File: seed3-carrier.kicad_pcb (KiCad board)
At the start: 2 copper layers, 49 parts, among them J1 AudioJack2, J2 AudioJack2, J3 5V_IN, J4 DISPLAY_UART, J5 SJ1-3535NG, U1 TLV9062IDR, U2 TPA6111A2DR

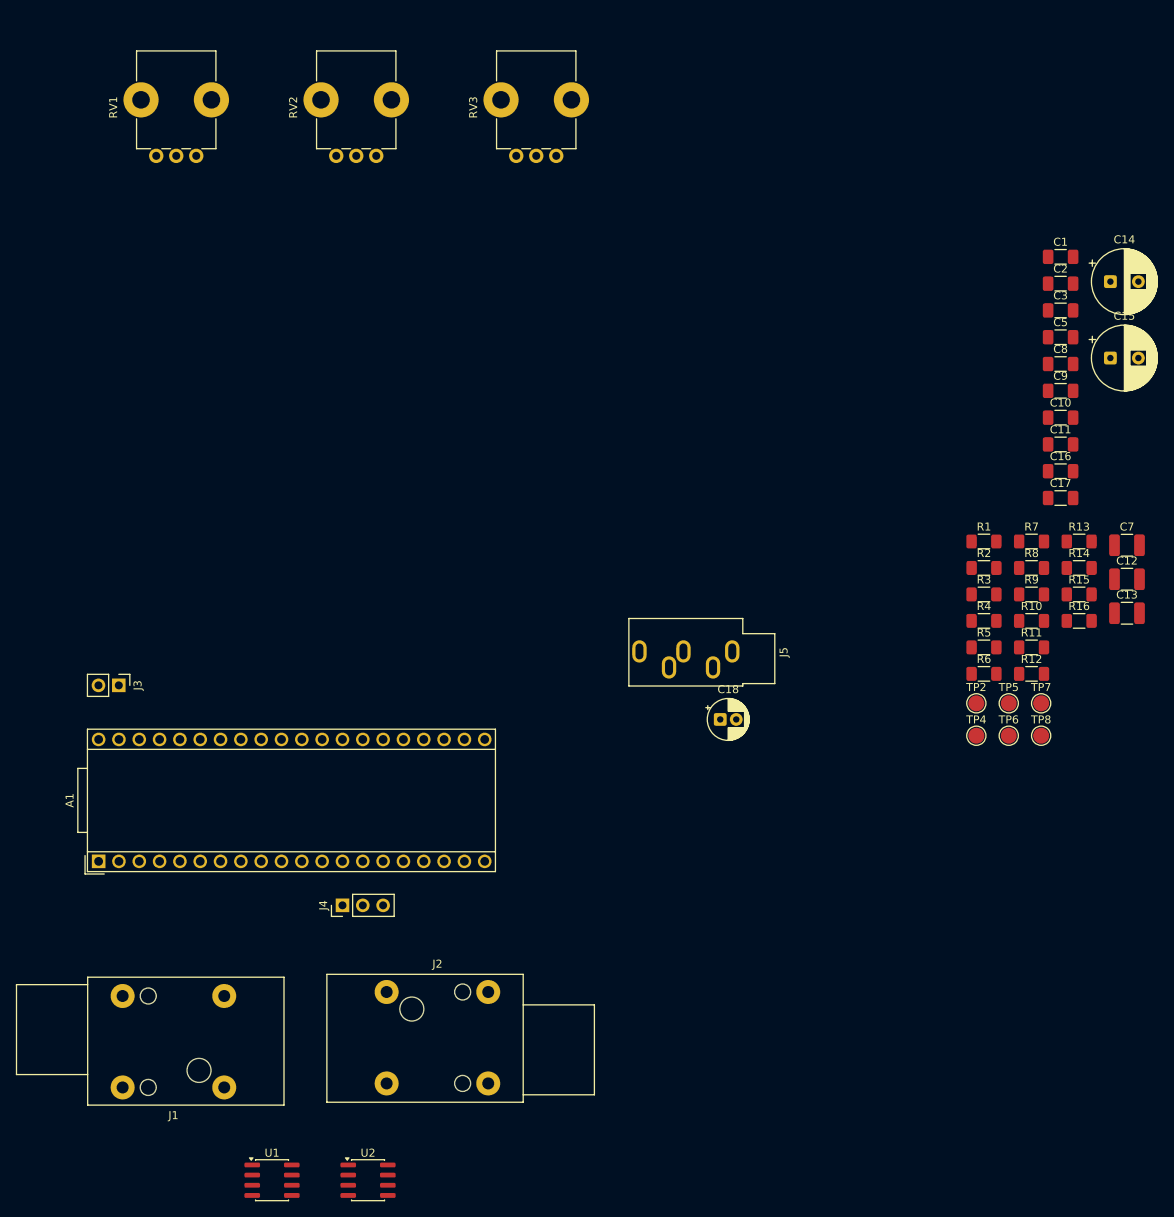
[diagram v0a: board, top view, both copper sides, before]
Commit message: Save initial PCB placement checkpoint
Capture preliminary component placement and schematic testpoint updates. Placement remains in progress; no copper traces or vias have been routed.
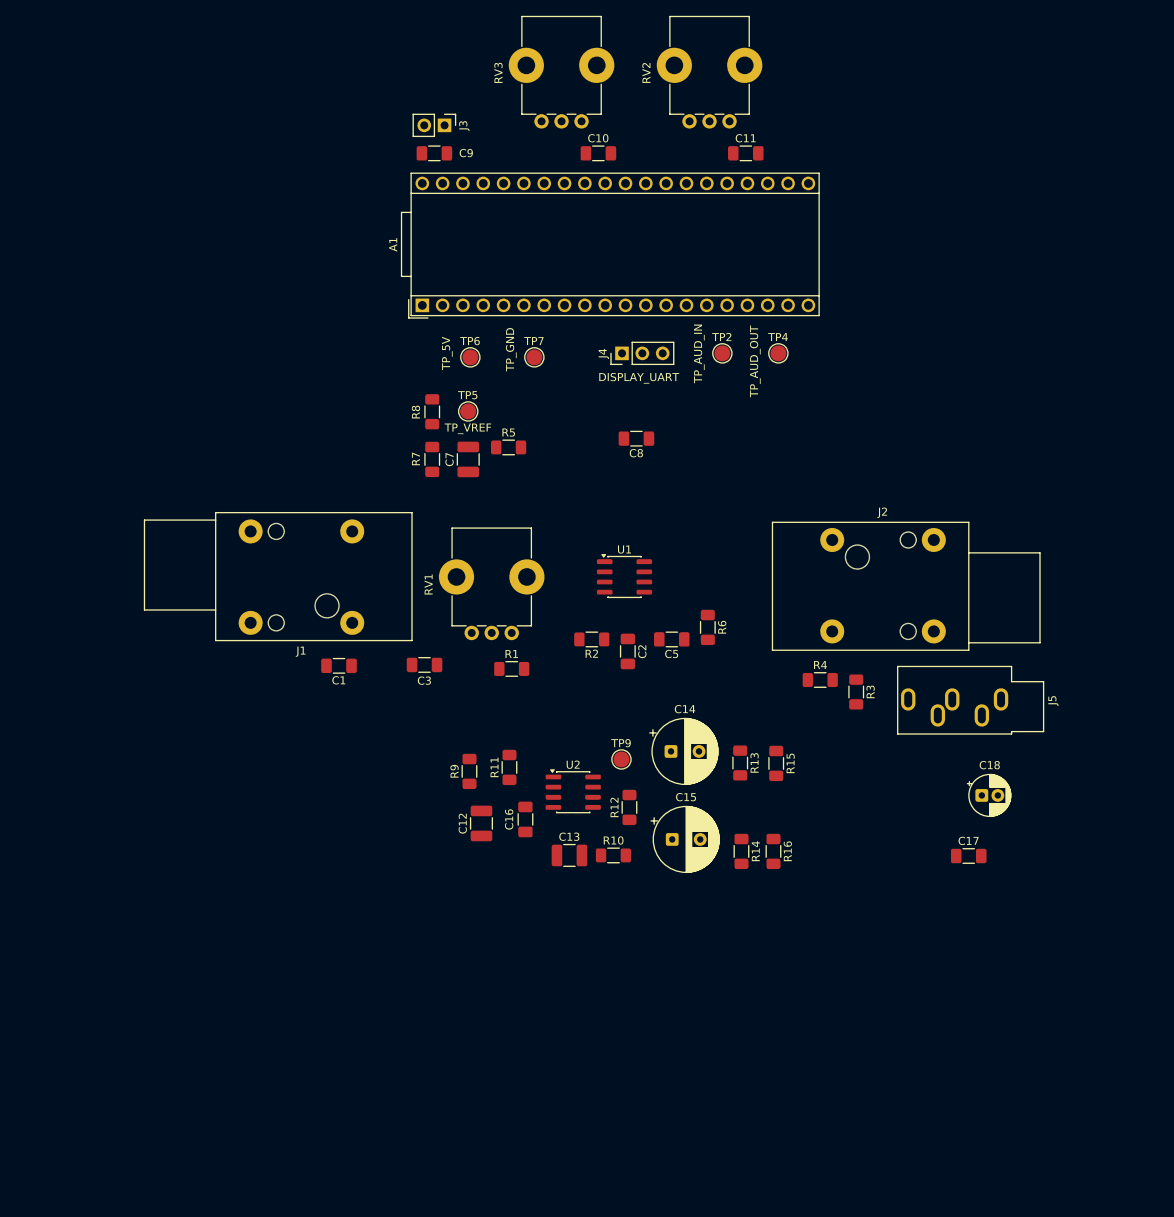
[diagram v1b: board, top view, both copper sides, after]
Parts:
- removed TP8: TestPoint, TestPoint:TestPoint_Pad_D2.0mm
- added TP9: TP_AMP_5V, TestPoint:TestPoint_Pad_D2.0mm, F.Cu at (114.7, 123.0)
- TP2: value TestPoint -> TP_AUD_IN
- TP4: value TestPoint -> TP_AUD_OUT
- TP5: value TestPoint -> TP_VREF
- TP6: value TestPoint -> TP_5V
- TP7: value TestPoint -> TP_GND
- moved C1 103.7 mm to (79.3, 111.3), turned to 180 degrees
- moved C3 91.0 mm to (90.0, 111.2)
- moved U1 87.3 mm to (115.0, 100.2)
- moved C12 86.3 mm to (97.2, 131.0), turned to 90 degrees
- moved C9 83.7 mm to (91.3, 47.2)
- moved C7 83.0 mm to (95.5, 85.5), turned to 90 degrees
- moved TP6 82.3 mm to (95.8, 72.7)
- moved C15 81.4 mm to (121.0, 133.0)
- moved J3 81.0 mm to (92.5, 43.7)
- moved A1 80.4 mm to (89.8, 66.2)
- moved C14 80.4 mm to (120.8, 122.0)
- moved C16 79.8 mm to (102.7, 130.5), turned to -90 degrees
- moved J2 79.3 mm to (141.0, 95.6)
- moved R8 77.4 mm to (91.0, 79.5), turned to -90 degrees
- moved J4 77.3 mm to (114.7, 72.2)
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
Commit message: Save PCB routing progress and Seed3 breakout headers
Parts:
- removed TP2: TP_AUD_IN, TestPoint:TestPoint_Pad_D2.0mm
- removed TP4: TP_AUD_OUT, TestPoint:TestPoint_Pad_D2.0mm
- removed TP6: TP_5V, TestPoint:TestPoint_Pad_D2.0mm
- removed TP7: TP_GND, TestPoint:TestPoint_Pad_D2.0mm
- added J6: Seed3_PINS_RIGHT, Connector_PinSocket_2.54mm:PinSocket_1x20_P2.54mm_Vertical, F.Cu at (101.0, 71.8)
- added J7: Seed3_PINS_LEFT, Connector_PinSocket_2.54mm:PinSocket_1x20_P2.54mm_Vertical, F.Cu at (101.0, 48.3)
- moved C17 62.2 mm to (119.4, 86.4), turned to 180 degrees
- moved C18 60.2 mm to (120.3, 81.9), turned to 180 degrees
- moved RV3 50.8 mm to (158.6, 56.9)
- moved C15 48.6 mm to (132.3, 85.7)
- moved C10 47.6 mm to (157.7, 59.7)
- moved R14 46.4 mm to (141.0, 89.5)
- moved R16 46.0 mm to (146.1, 90.2)
- moved C12 39.1 mm to (108.9, 93.7)
- moved C13 39.0 mm to (118.9, 97.5)
- moved R10 39.0 mm to (124.4, 97.5)
- moved R9 38.4 mm to (108.2, 88.2)
- moved R12 38.3 mm to (124.7, 91.8)
- moved R11 38.2 mm to (112.7, 87.7)
- moved C16 38.0 mm to (113.9, 94.2)
- moved TP9 37.8 mm to (125.4, 86.7)
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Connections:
- net /AUDIO_IN renamed /AUDIO_IN_1
- net /AUDIO_OUT renamed /AUDIO_OUT_1
- A1 pad 1: unconnected-(A1-USB_ID-Pad1) -> /D0
- A1 pad 10: unconnected-(A1-SPI1_POCI-Pad10) -> /D9
- A1 pad 11: unconnected-(A1-SPI1_PICO-Pad11) -> /D10
- A1 pad 12: unconnected-(A1-I2C1_SCL-Pad12) -> /D11
- A1 pad 13: unconnected-(A1-I2C1_SDA-Pad13) -> /D12
- A1 pad 17: unconnected-(A1-AUDIO_IN_2-Pad17) -> /AUDIO_IN_2
- A1 pad 19: unconnected-(A1-AUDIO_OUT_2-Pad19) -> /AUDIO_OUT_2
- A1 pad 2: unconnected-(A1-SD_DATA_3-Pad2) -> /D1
- A1 pad 24: unconnected-(A1-ADC_2-Pad24) -> /A2
- A1 pad 25: unconnected-(A1-ADC_3-Pad25) -> /A3
- A1 pad 26: unconnected-(A1-ADC_4-Pad26) -> /A4
- A1 pad 27: unconnected-(A1-ADC_5-Pad27) -> /A5
- A1 pad 28: unconnected-(A1-ADC_6-Pad28) -> /A6
- A1 pad 29: unconnected-(A1-DAC_OUT2-Pad29) -> /A7
- A1 pad 3: unconnected-(A1-SD_DATA_2-Pad3) -> /D2
- A1 pad 30: unconnected-(A1-DAC_OUT1-Pad30) -> /A8
- A1 pad 31: unconnected-(A1-SAI2_MCLK-Pad31) -> /A9
- A1 pad 32: unconnected-(A1-SAI2_SD_B-Pad32) -> /A10
- A1 pad 33: unconnected-(A1-SAI2_SD_A-Pad33) -> /D26
- A1 pad 34: unconnected-(A1-SAI2_FS-Pad34) -> /D27
- A1 pad 35: unconnected-(A1-SAI2_SCK-Pad35) -> /A11
- A1 pad 36: unconnected-(A1-USB_D_--Pad36) -> /USB_D-
- A1 pad 37: unconnected-(A1-USB_D_+-Pad37) -> /USB_D+
- A1 pad 38: unconnected-(A1-3V3_D-Pad38) -> /3V3_D
- A1 pad 4: unconnected-(A1-SD_DATA_1-Pad4) -> /D3
- A1 pad 5: unconnected-(A1-SD_DATA_0-Pad5) -> /D4
- A1 pad 6: unconnected-(A1-SD_CMD-Pad6) -> /D5
- A1 pad 7: unconnected-(A1-SD_CLK-Pad7) -> /D6
- A1 pad 8: unconnected-(A1-SPI1_CS-Pad8) -> /D7
- A1 pad 9: unconnected-(A1-SPI1_SCK-Pad9) -> /D8
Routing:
- net +5V: track 0.00 -> 116.2 mm
- net /TONE_POT: track 0.00 -> 73.7 mm
- net /3V3_A: track 0.00 -> 62.9 mm
- net /VREF: track 0.00 -> 55.2 mm, vias 0 -> 2
- net /VOLUME_POT: track 0.00 -> 49.6 mm
- net /HP_SOURCE: track 0.00 -> 29.2 mm
- net Net-(U2-VOUT1): track 0.00 -> 25.7 mm, vias 0 -> 2
- net Net-(J2-PadT): track 0.00 -> 22.6 mm
- net /HP_L: track 0.00 -> 16.9 mm
- net Net-(C1-Pad1): track 0.00 -> 16.1 mm
- net /AUDIO_IN_1: track 0.00 -> 14.7 mm
- net /HP_R: track 0.00 -> 13.0 mm
- net /AUDIO_OUT_1: track 0.00 -> 12.4 mm
- net GND: track 0.00 -> 12.1 mm
- net Net-(C15-Pad2): track 0.00 -> 11.4 mm
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- added copper zone on B.Cu, net GND
- added copper zone on F.Cu, net GND
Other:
- board outline added: 113 x 61.6 mm
- board text added: "5V"
- board text added: "<-- 5V INPUT :D"
- board text added: "GND"
- board text added: "RX"
- board text added: "TX"

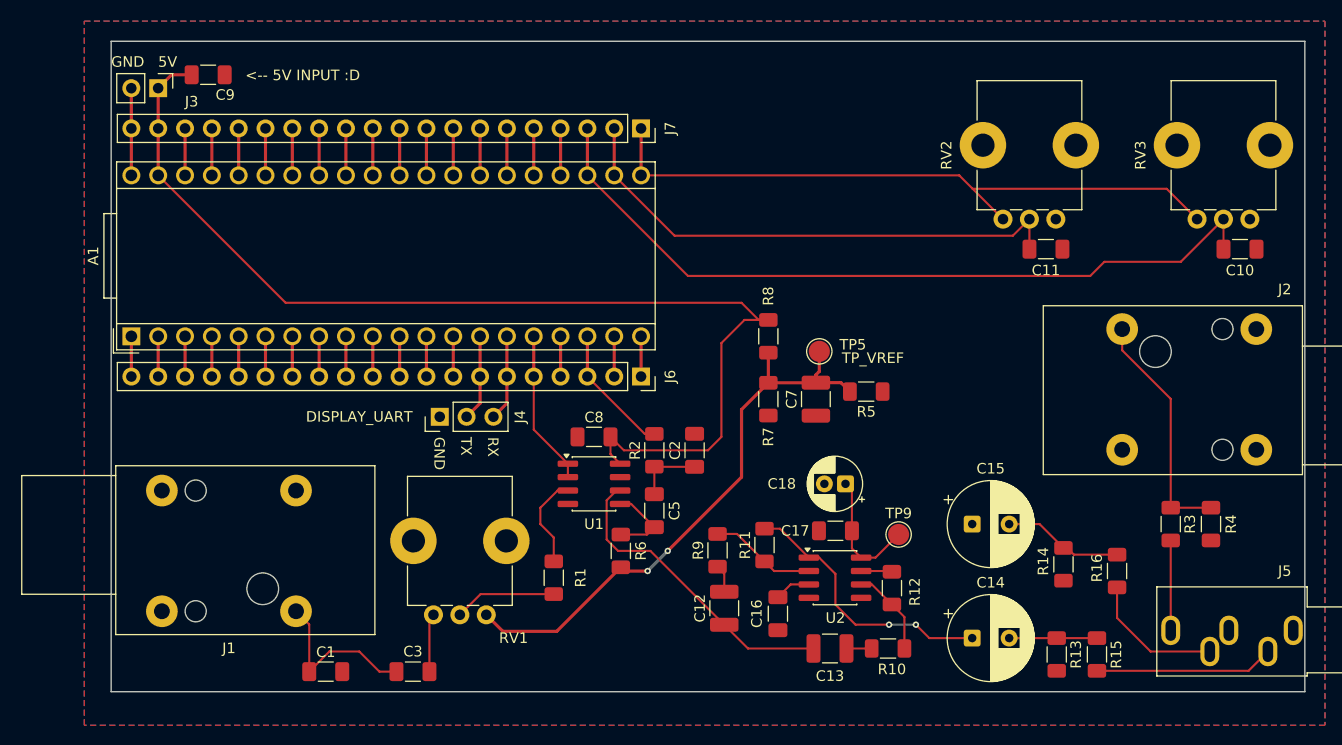
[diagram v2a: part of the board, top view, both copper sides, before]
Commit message: Save ground pours and stitching via placement
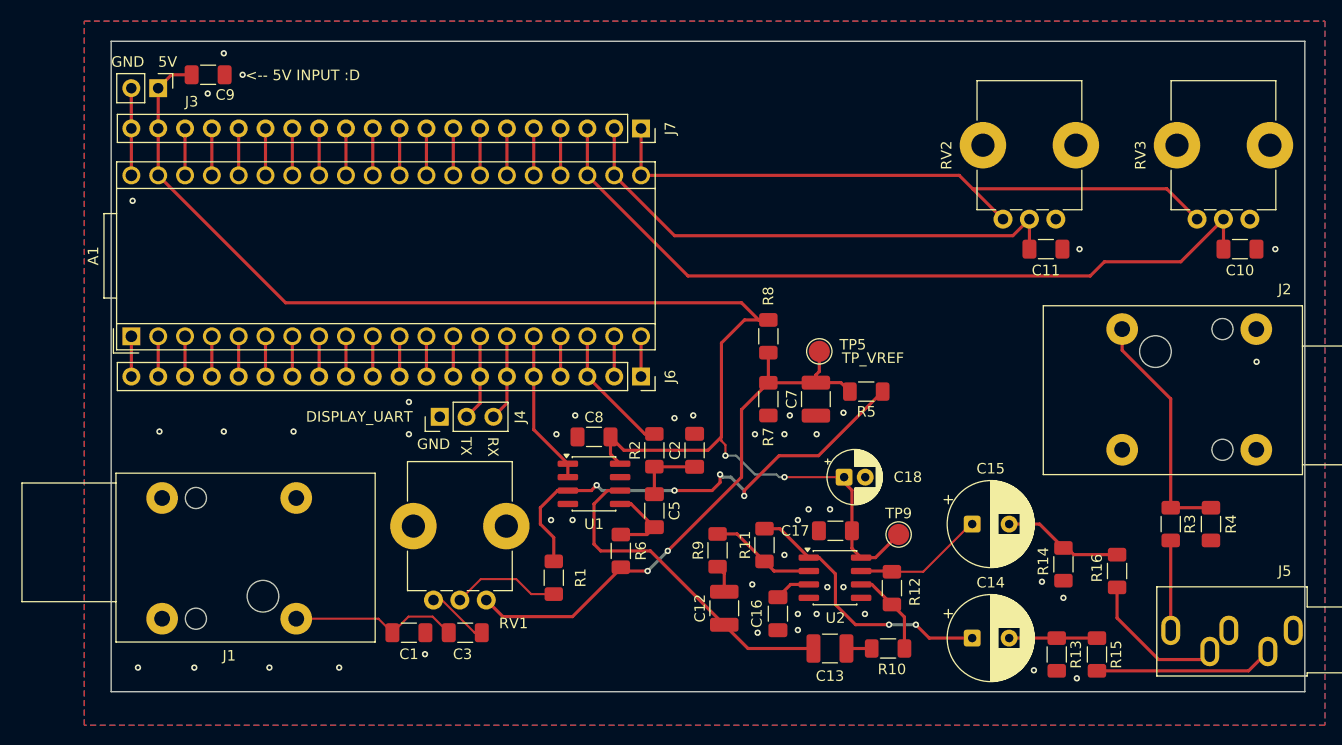
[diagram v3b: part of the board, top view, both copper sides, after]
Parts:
- moved C1 8.69 mm to (79.0, 96.0)
- moved C3 6.17 mm to (84.3, 96.0)
- moved RV1 1.40 mm to (86.3, 92.9)
- moved J1 0.71 mm to (68.3, 94.7)
- moved C18 0.65 mm to (120.2, 81.3), turned to 0 degrees
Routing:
- net Net-(U1A-+): track 8.88 -> 45.7 mm, vias 0 -> 4
- net +5V: track 116.2 -> 130.2 mm, vias 0 -> 2
- net Net-(U2-VOUT2): track 2.94 -> 12.4 mm
- net /HP_SOURCE: track 29.2 -> 31.7 mm
- net /HP_R: track 13.0 -> 13.6 mm
- net Net-(R1-Pad1): track 9.70 -> 10.3 mm
- net /VREF: track 55.2 -> 54.7 mm
- net GND: vias 0 -> 44

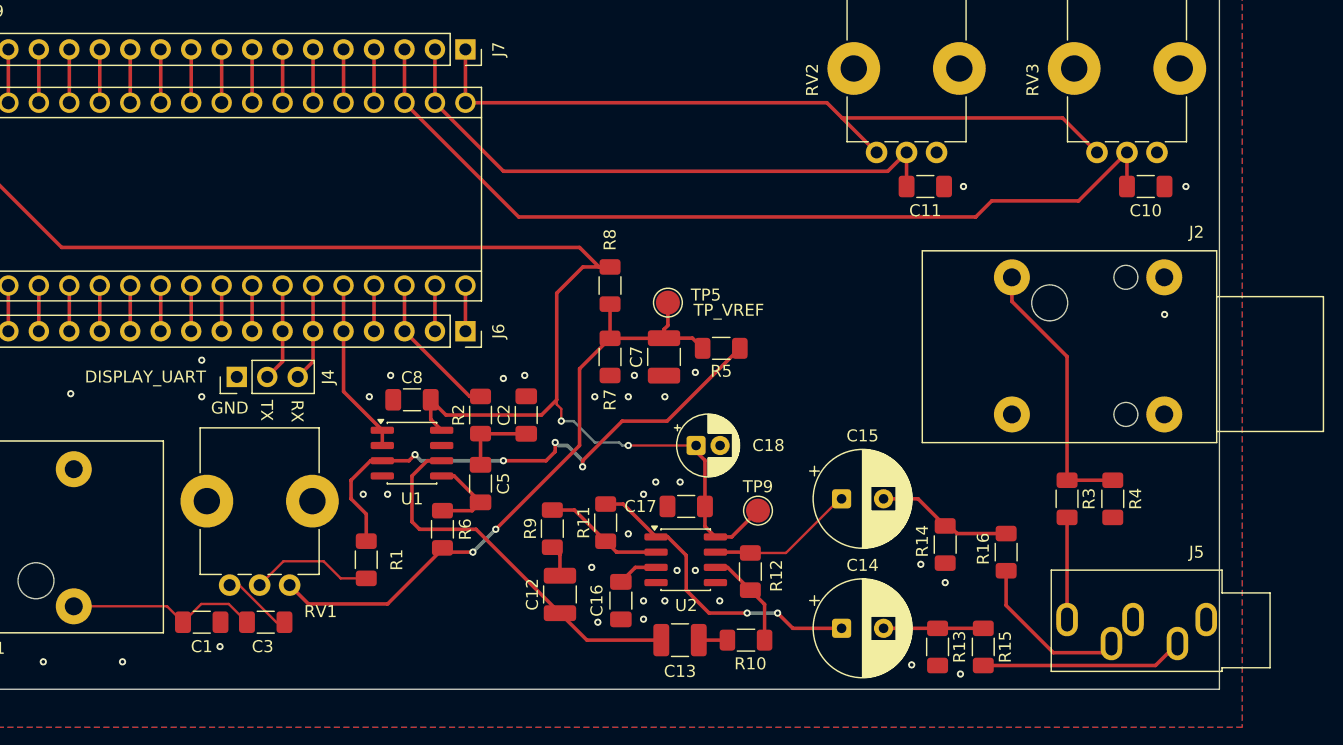
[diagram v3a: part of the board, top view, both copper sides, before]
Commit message: Improve PCB routing and enforce 0.30 mm minimum track width
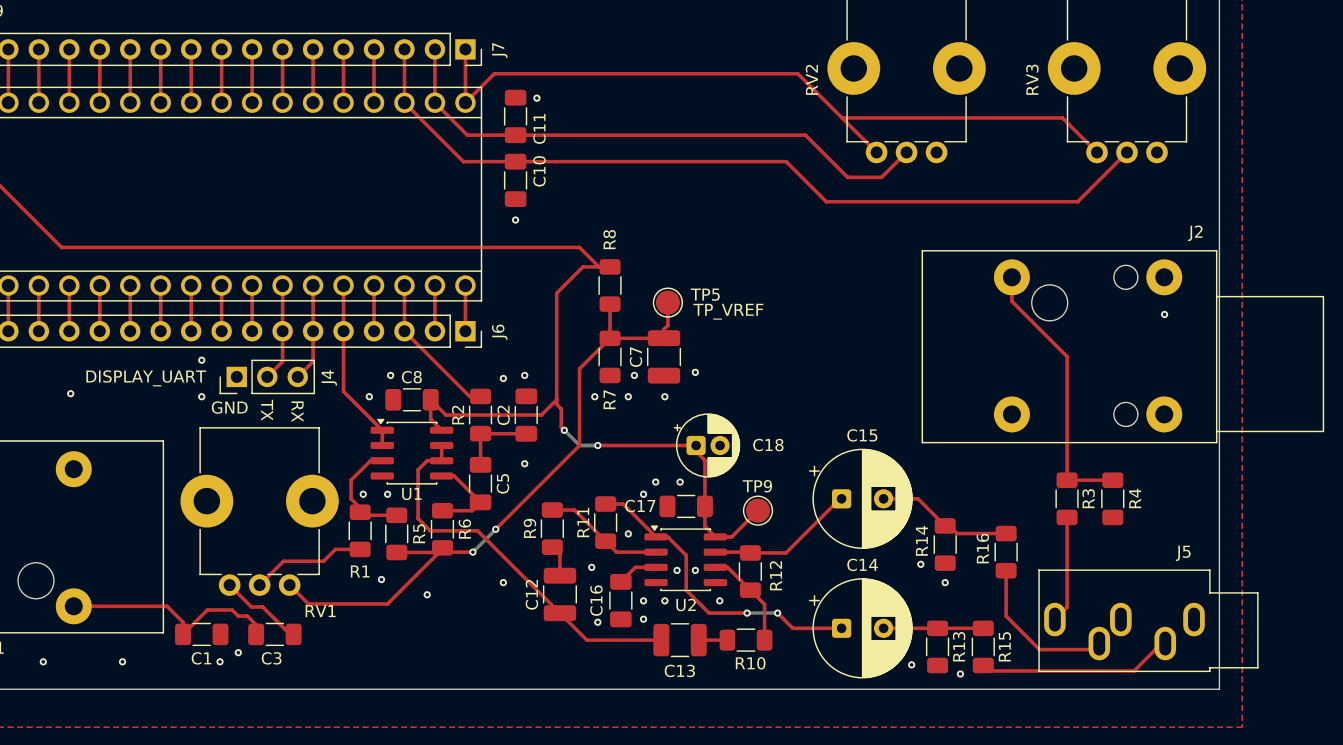
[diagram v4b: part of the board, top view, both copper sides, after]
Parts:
- moved C10 52.5 mm to (105.2, 59.2), turned to -90 degrees
- moved C11 34.7 mm to (105.2, 53.8), turned to 90 degrees
- moved R5 31.2 mm to (95.2, 88.6), turned to 90 degrees
- moved R1 2.47 mm to (92.2, 88.4)
- moved C3 1.27 mm to (85.1, 97.0)
- moved C1 1.02 mm to (79.0, 97.0)
- moved J5 1.02 mm to (161.7, 95.8)
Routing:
- net Net-(U1A-+): track 45.7 -> 9.20 mm, vias 4 -> 0
- net /TONE_POT: track 73.7 -> 69.8 mm
- net Net-(C1-Pad1): track 16.3 -> 18.9 mm
- net /VOLUME_POT: track 49.6 -> 47.2 mm
- net /3V3_A: track 62.9 -> 64.9 mm
- net Net-(C3-Pad2): track 5.85 -> 7.03 mm
- net /HP_R: track 13.6 -> 12.9 mm
- net Net-(R1-Pad1): track 10.3 -> 9.61 mm
- net /HP_L: track 16.9 -> 16.3 mm
- net GND: vias 44 -> 49
